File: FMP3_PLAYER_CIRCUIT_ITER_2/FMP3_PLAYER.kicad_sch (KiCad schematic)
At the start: 47 parts, among them J1 USB_C_Receptacle_PowerOnly_6P, J2 AudioJack3, J3 ISP, Q1 PMOS, Q2 PMOS, SW1 SW_L, SW2 SW_D, SW3 SW_R, SW4 SW_U, SW5 SW_SPDT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

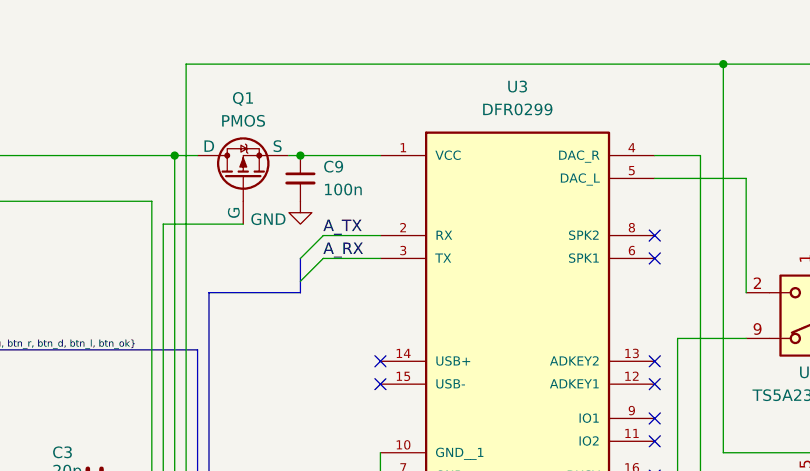
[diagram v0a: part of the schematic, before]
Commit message: The DFPlayer NEEDS a fat decoupling cap...
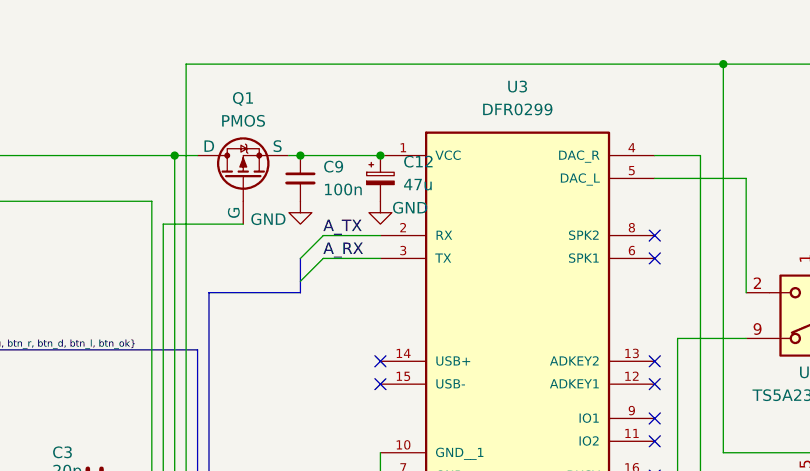
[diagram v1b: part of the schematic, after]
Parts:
- added C12: 47u, Capacitor_THT:CP_Radial_D5.0mm_P2.50mm, symbol Device:C_Polarized_Small
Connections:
- net GND: now also C12.2
- net at C9.1, Q1.3 (S), U3.1 (VCC): now also C12.1
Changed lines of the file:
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@@
 	)
 	(junction
+		(at 208.28 27.94)
+		(diameter 0)
+		(color 0 0 0 0)
+	)
+	(junction
 		(at 185.42 109.22)
 		(diameter 0)
@@
 	)
 	(symbol
+		(lib_id "power:GND")
+		(at 208.28 33.02 0)
+		(unit 1)
+		(exclude_from_sim no)
+		(in_bom yes)
+		(on_board yes)
+		(dnp no)
+		(property "Reference" "#PWR033"
+			(at 208.28 39.37 0)
+			(effects
+				(font
+					(size 1.27 1.27)
+				)
+				(hide yes)
+			)
+		)
+		(property "Value" "GND"
+			(at 211.582 33.782 0)
+			(effects
+				(font
+					(size 1.27 1.27)
+				)
+			)
+		)
+		(property "Footprint" ""
+			(at 208.28 33.02 0)
+			(effects
+				(font
+					(size 1.27 1.27)
+				)
+				(hide yes)
+			)
+		)
+		(property "Datasheet" ""
+			(at 208.28 33.02 0)
+			(effects
+				(font
+					(size 1.27 1.27)
+				)
+				(hide yes)
+			)
+		)
+		(property "Description" "Power symbol creates a global label with name \"GND\" , ground"
+			(at 208.28 33.02 0)
+			(effects
+				(font
+					(size 1.27 1.27)
+				)
+				(hide yes)
+			)
+		)
+		(pin "1"
+		)
+		(instances
+			(project "FMP3_PLAYER"
+				(path "/a3d3848e-8dd1-4cdc-911f-454b6af41ad0"
+					(reference "#PWR033")
+					(unit 1)
+				)
+			)
+		)
+	)
+	(symbol
 		(lib_id "Device:R")
 		(at 189.23 111.76 90)
@@
 					(unit 1)
 				)
+			)
+		)
+	)
+	(symbol
+		(lib_id "Device:C_Polarized_Small")
+		(at 208.28 30.48 0)
+		(unit 1)
+		(exclude_from_sim no)
+		(in_bom yes)
+		(on_board yes)
+		(dnp no)
+		(fields_autoplaced yes)
+		(property "Reference" "C12"
+			(at 210.82 28.6638 0)
+			(effects
+				(font
+					(size 1.27 1.27)
+				)
+				(justify left)
+			)
+		)
+		(property "Value" "47u"
+			(at 210.82 31.2038 0)
+			(effects
+				(font
+					(size 1.27 1.27)
+				)
+				(justify left)
+			)
+		)
+		(property "Footprint" "Capacitor_THT:CP_Radial_D5.0mm_P2.50mm"
+			(at 208.28 30.48 0)
+			(effects
+				(font
+					(size 1.27 1.27)
+				)
+				(hide yes)
+			)
+		)
+		(property "Datasheet" "~"
+			(at 208.28 30.48 0)
+			(effects
+				(font
+					(size 1.27 1.27)
+				)
+				(hide yes)
+			)
+		)
+		(property "Description" "Polarized capacitor, small symbol"
+			(at 208.28 30.48 0)
+			(effects
+				(font
+					(size 1.27 1.27)
+				)
+				(hide yes)
+			)
+		)
+		(pin "2"
+		)
+		(pin "1"
+		)
+		(instances
+			(project ""
+				(path "/a3d3848e-8dd1-4cdc-911f-454b6af41ad0"
+					(reference "C12")
+					(unit 1)
+				)

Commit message: I swear to git this is the final pcb...
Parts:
- added C13, C14: 100n, Capacitor_SMD:C_0805_2012Metric_Pad1.18x1.45mm_HandSolder, symbol Device:C_Small
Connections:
- net at J2.R: now also C14.1; no longer U4.6
- net at J2.T: now also C13.1; no longer U4.10
- new net: C14.2, U4.6
- new net: C13.2, U4.10
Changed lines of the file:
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@@
 	(wire
 		(pts
+			(xy 264.16 27.94) (xy 264.16 40.64)
+		)
+		(stroke
+			(width 0)
+			(type default)
+		)
+	)
+	(wire
+		(pts
 			(xy 233.68 82.55) (xy 241.3 82.55)
 		)
@@
 	(wire
 		(pts
-			(xy 266.7 68.58) (xy 266.7 30.48)
-		)
-		(stroke
-			(width 0)
-			(type default)
-		)
-	)
-	(wire
-		(pts
 			(xy 50.8 36.83) (xy 48.26 36.83)
 		)
@@
 	(wire
 		(pts
-			(xy 264.16 45.72) (xy 264.16 27.94)
-		)
-		(stroke
-			(width 0)
-			(type default)
-		)
-	)
-	(wire
-		(pts
 			(xy 212.09 144.78) (xy 212.09 154.94)
 		)
@@
 	(wire
 		(pts
+			(xy 266.7 30.48) (xy 266.7 63.5)
+		)
+		(stroke
+			(width 0)
+			(type default)
+		)
+	)
+	(wire
+		(pts
 			(xy 149.86 27.94) (xy 185.42 27.94)
 		)
@@
 	(symbol
 		(lib_id "Device:C_Small")
+		(at 266.7 66.04 0)
+		(unit 1)
+		(exclude_from_sim no)
+		(in_bom yes)
+		(on_board yes)
+		(dnp no)
+		(property "Reference" "C14"
+			(at 269.24 64.7762 0)
+			(effects
+				(font
+					(size 1.27 1.27)
+				)
+				(justify left)
+			)
+		)
+		(property "Value" "100n"
+			(at 269.24 67.3162 0)
+			(effects
+				(font
+					(size 1.27 1.27)
+				)
+				(justify left)
+			)
+		)
+		(property "Footprint" "Capacitor_SMD:C_0805_2012Metric_Pad1.18x1.45mm_HandSolder"
+			(at 266.7 66.04 0)
+			(effects
+				(font
+					(size 1.27 1.27)
+				)
+				(hide yes)
+			)
+		)
+		(property "Datasheet" "~"
+			(at 266.7 66.04 0)
+			(effects
+				(font
+					(size 1.27 1.27)
+				)
+				(hide yes)
+			)
+		)
+		(property "Description" "Unpolarized capacitor, small symbol"
+			(at 266.7 66.04 0)
+			(effects
+				(font
+					(size 1.27 1.27)
+				)
+				(hide yes)
+			)
+		)
+		(pin "2"
+		)
+		(pin "1"
+		)
+		(instances
+			(project "FMP3_PLAYER"
+				(path "/a3d3848e-8dd1-4cdc-911f-454b6af41ad0"
+					(reference "C14")
+					(unit 1)
+				)
+			)
+		)
+	)
+	(symbol
+		(lib_id "Device:C_Small")
 		(at 140.97 31.75 90)
 		(unit 1)
@@
 					(unit 1)
 				)
+			)
+		)
+	)
+	(symbol
+		(lib_id "Device:C_Small")
+		(at 264.16 43.18 0)
+		(unit 1)
+		(exclude_from_sim no)
+		(in_bom yes)
+		(on_board yes)
+		(dnp no)
+		(property "Reference" "C13"
+			(at 258.826 37.592 0)
+			(effects
+				(font
+					(size 1.27 1.27)
+				)
+				(justify left)
+			)
+		)
+		(property "Value" "100n"
+			(at 258.826 40.132 0)
+			(effects
+				(font
+					(size 1.27 1.27)
+				)
+				(justify left)
+			)
+		)
+		(property "Footprint" "Capacitor_SMD:C_0805_2012Metric_Pad1.18x1.45mm_HandSolder"
+			(at 264.16 43.18 0)
+			(effects
+				(font
+					(size 1.27 1.27)
+				)
+				(hide yes)
+			)
+		)
+		(property "Datasheet" "~"
+			(at 264.16 43.18 0)
+			(effects
+				(font
+					(size 1.27 1.27)
+				)
+				(hide yes)
+			)
+		)
+		(property "Description" "Unpolarized capacitor, small symbol"
+			(at 264.16 43.18 0)
+			(effects
+				(font
+					(size 1.27 1.27)
+				)
+				(hide yes)
+			)
+		)
+		(pin "2"
+		)
+		(pin "1"
+		)
+		(instances
+			(project "FMP3_PLAYER"
+				(path "/a3d3848e-8dd1-4cdc-911f-454b6af41ad0"
+					(reference "C13")
+					(unit 1)
+				)

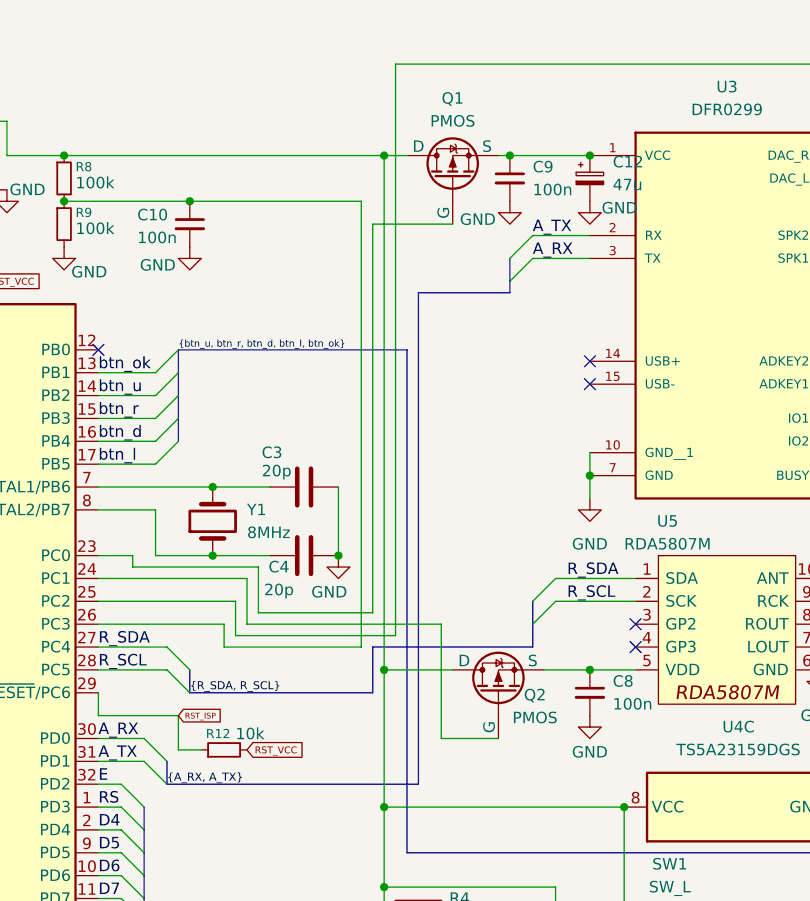
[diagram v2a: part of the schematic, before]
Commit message: I realized after some prototyping my PMOS was bad, fixed now, i swear this better be the final...
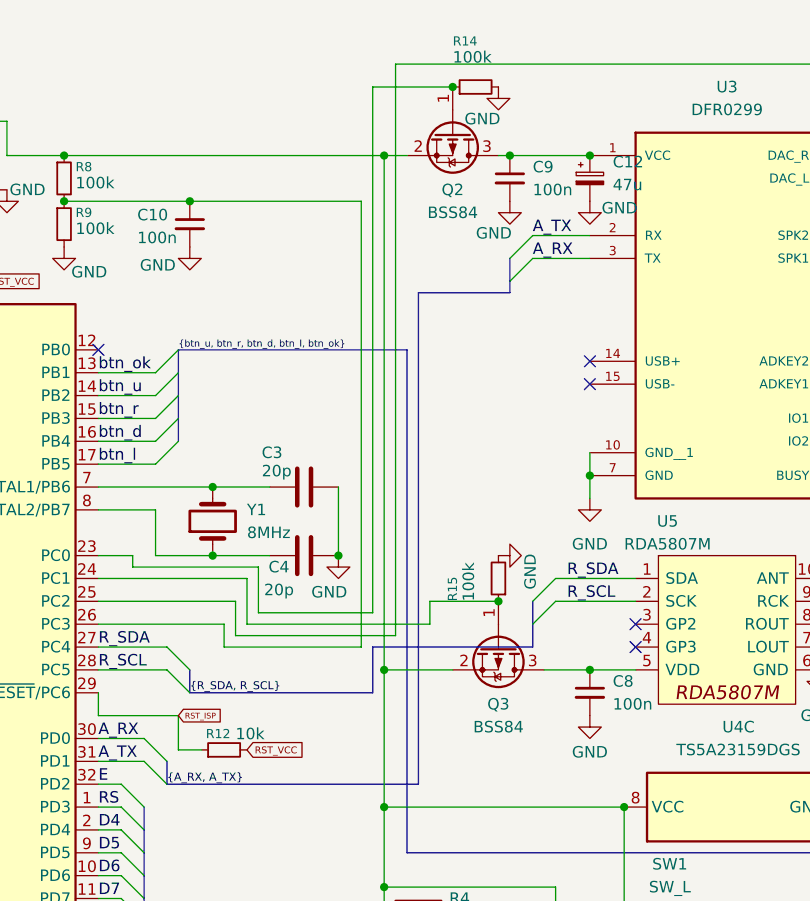
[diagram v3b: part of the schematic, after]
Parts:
- removed Q1, Q2: PMOS, Package_TO_SOT_SMD:SOT-23_Handsoldering, symbol Simulation_SPICE:PMOS
- added Q2, Q3: BSS84, Package_TO_SOT_SMD:SOT-23_Handsoldering, symbol Transistor_FET:BSS84
- added R14, R15: 100k, Resistor_SMD:R_0805_2012Metric_Pad1.20x1.40mm_HandSolder, symbol Device:R_Small
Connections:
- net GND: now also R14.2, R15.2
- net at C8.1, U5.5 (VDD): now also Q3.3 (D)
- net at C5.1, DS1.2 (VDD), R4.1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: now also Q2.2 (S), Q3.2 (S)
- net at U1.23 (PC0): now also Q2.1 (G), R14.1
- net at U1.24 (PC1): now also Q3.1 (G), R15.1
- net at C12.1, C9.1, U3.1 (VCC): now also Q2.3 (D)

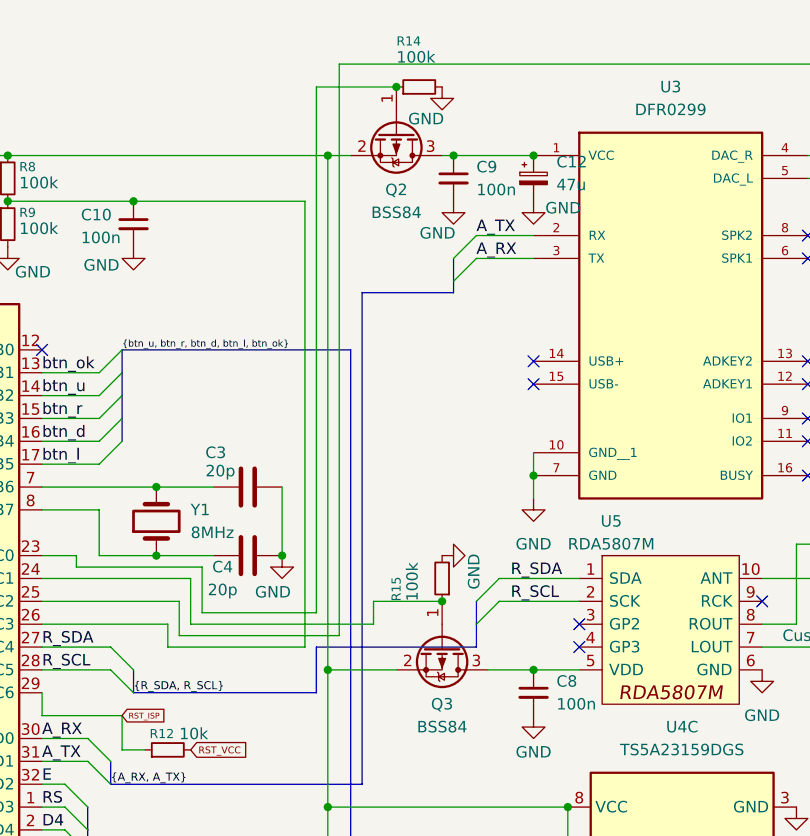
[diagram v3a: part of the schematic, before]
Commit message: minor fix, used pulldowns instead of pullups by accident
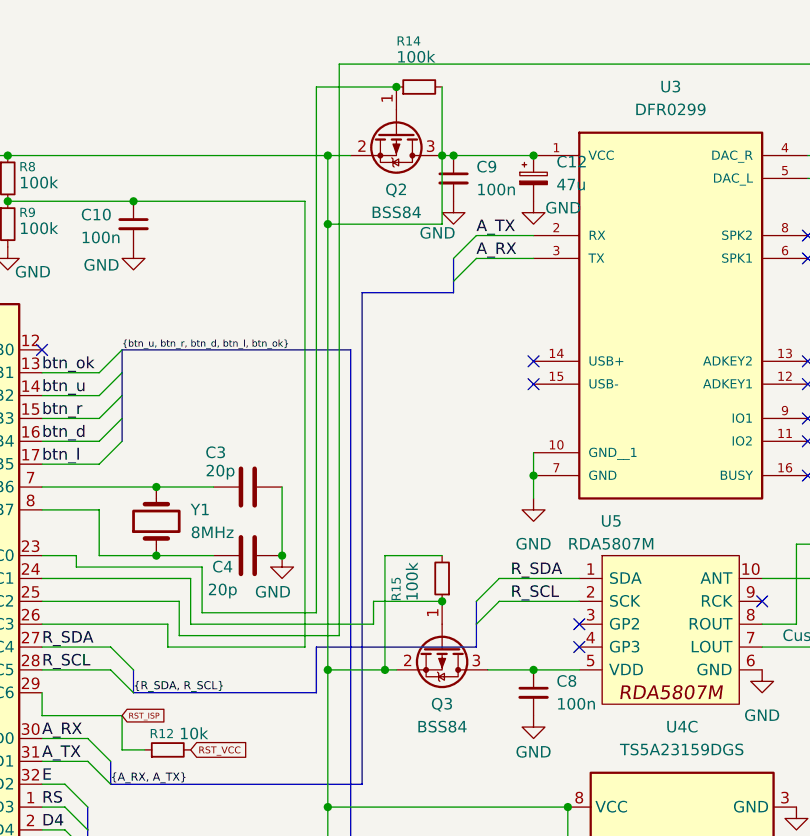
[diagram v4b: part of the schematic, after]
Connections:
- net GND: no longer R14.2, R15.2
- net at C5.1, DS1.2 (VDD), Q2.2 (S)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: now also C12.1, C9.1, Q2.3 (D), R14.2, R15.2, U3.1 (VCC)
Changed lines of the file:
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@@
 	)
 	(junction
+		(at 198.12 27.94)
+		(diameter 0)
+		(color 0 0 0 0)
+	)
+	(junction
 		(at 226.06 134.62)
 		(diameter 0)
@@
 	)
 	(junction
+		(at 191.77 85.09)
+		(diameter 0)
+		(color 0 0 0 0)
+	)
+	(junction
 		(at 208.28 63.5)
 		(diameter 0)
@@
 	)
 	(junction
+		(at 185.42 35.56)
+		(diameter 0)
+		(color 0 0 0 0)
+	)
+	(junction
 		(at 166.37 72.39)
 		(diameter 0)
@@
 	(wire
 		(pts
+			(xy 198.12 27.94) (xy 198.12 35.56)
+		)
+		(stroke
+			(width 0)
+			(type default)
+		)
+	)
+	(wire
+		(pts
 			(xy 168.91 77.47) (xy 168.91 81.28)
 		)
@@
 	(wire
 		(pts
+			(xy 185.42 35.56) (xy 185.42 85.09)
+		)
+		(stroke
+			(width 0)
+			(type default)
+		)
+	)
+	(wire
+		(pts
 			(xy 173.99 119.38) (xy 173.99 123.19)
 		)
@@
 	(wire
 		(pts
+			(xy 191.77 85.09) (xy 193.04 85.09)
+		)
+		(stroke
+			(width 0)
+			(type default)
+		)
+	)
+	(wire
+		(pts
 			(xy 198.12 111.76) (xy 198.12 124.46)
 		)
@@
 	(wire
 		(pts
-			(xy 185.42 85.09) (xy 193.04 85.09)
+			(xy 185.42 85.09) (xy 191.77 85.09)
 		)
 		(stroke
@@
 	(wire
 		(pts
-			(xy 185.42 27.94) (xy 185.42 85.09)
+			(xy 185.42 27.94) (xy 185.42 35.56)
 		)
 		(stroke
@@
 	(wire
 		(pts
+			(xy 191.77 72.39) (xy 191.77 85.09)
+		)
+		(stroke
+			(width 0)
+			(type default)
+		)
+	)
+	(wire
+		(pts
 			(xy 248.92 30.48) (xy 248.92 43.18)
 		)
@@
 	(wire
 		(pts
+			(xy 198.12 72.39) (xy 191.77 72.39)
+		)
+		(stroke
+			(width 0)
+			(type default)
+		)
+	)
+	(wire
+		(pts
 			(xy 233.68 133.35) (xy 233.68 144.78)
 		)
@@
 	(wire
 		(pts
+			(xy 198.12 20.32) (xy 198.12 27.94)
+		)
+		(stroke
+			(width 0)
+			(type default)
+		)
+	)
+	(wire
+		(pts
 			(xy 153.67 62.23) (xy 160.02 62.23)
 		)
@@
 	(wire
 		(pts
+			(xy 198.12 35.56) (xy 185.42 35.56)
+		)
+		(stroke
+			(width 0)
+			(type default)
+		)
+	)
+	(wire
+		(pts
 			(xy 149.86 27.94) (xy 185.42 27.94)
 		)
@@
 	(symbol
 		(lib_id "power:GND")
-		(at 198.12 20.32 0)
-		(unit 1)
-		(exclude_from_sim no)
-		(in_bom yes)
-		(on_board yes)
-		(dnp no)
-		(property "Reference" "#PWR034"
-			(at 198.12 26.67 0)
-			(effects
-				(font
-					(size 1.27 1.27)
-				)
-				(hide yes)
-			)
-		)
-		(property "Value" "GND"
-			(at 196.342 23.876 0)
-			(effects
-				(font
-					(size 1.27 1.27)
-				)
-			)
-		)
-		(property "Footprint" ""
-			(at 198.12 20.32 0)
-			(effects
-				(font
-					(size 1.27 1.27)
-				)
-				(hide yes)
-			)
-		)
-		(property "Datasheet" ""
-			(at 198.12 20.32 0)
-			(effects
-				(font
-					(size 1.27 1.27)
-				)
-				(hide yes)
-			)
-		)
-		(property "Description" "Power symbol creates a global label with name \"GND\" , ground"
-			(at 198.12 20.32 0)
-			(effects
-				(font
-					(size 1.27 1.27)
-				)
-				(hide yes)
-			)
-		)
-		(pin "1"
-		)
-		(instances
-			(project "FMP3_PLAYER"
-				(path "/a3d3848e-8dd1-4cdc-911f-454b6af41ad0"
-					(reference "#PWR034")
-					(unit 1)
-				)
-			)
-		)
-	)
-	(symbol
-		(lib_id "power:GND")
 		(at 208.28 33.02 0)
 		(unit 1)
@@
 					(unit 1)
 				)
-			)
-		)
-	)
-	(symbol
-		(lib_id "power:GND")
-		(at 198.12 72.39 90)
-		(unit 1)
-		(exclude_from_sim no)
-		(in_bom yes)
-		(on_board yes)
-		(dnp no)
-		(property "Reference" "#PWR035"
-			(at 204.47 72.39 0)
-			(effects
-				(font
-					(size 1.27 1.27)
-				)
-				(hide yes)
-			)
-		)
-		(property "Value" "GND"
-			(at 201.676 74.168 0)
-			(effects
-				(font
-					(size 1.27 1.27)
-				)
-			)
-		)
-		(property "Footprint" ""
-			(at 198.12 72.39 0)
-			(effects
-				(font
-					(size 1.27 1.27)
-				)
-				(hide yes)
-			)
-		)
-		(property "Datasheet" ""
-			(at 198.12 72.39 0)
-			(effects
-				(font
-					(size 1.27 1.27)
-				)
-				(hide yes)
-			)
-		)
-		(property "Description" "Power symbol creates a global label with name \"GND\" , ground"
-			(at 198.12 72.39 0)
-			(effects
-				(font
-					(size 1.27 1.27)
-				)
-				(hide yes)
-			)
-		)
-		(pin "1"
-		)
-		(instances
-			(project "FMP3_PLAYER"
-				(path "/a3d3848e-8dd1-4cdc-911f-454b6af41ad0"
-					(reference "#PWR035")
-					(unit 1)
-				)

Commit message: another minor fix, i should really go sleep...
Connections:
- net at C5.1, DS1.2 (VDD), Q2.2 (S)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: no longer C12.1, C9.1, Q2.3 (D), U3.1 (VCC)
- new net: C12.1, C9.1, Q2.3 (D), U3.1 (VCC)
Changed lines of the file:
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@@
-	)
-	(junction
-		(at 198.12 27.94)
-		(diameter 0)
-		(color 0 0 0 0)
 	)
 	(junction
@@
 	(wire
 		(pts
-			(xy 198.12 27.94) (xy 198.12 35.56)
+			(xy 201.93 20.32) (xy 201.93 35.56)
 		)
 		(stroke
@@
 	(wire
 		(pts
-			(xy 198.12 20.32) (xy 198.12 27.94)
-		)
-		(stroke
-			(width 0)
-			(type default)
-		)
-	)
-	(wire
-		(pts
 			(xy 153.67 62.23) (xy 160.02 62.23)
 		)
@@
 	(wire
 		(pts
-			(xy 198.12 35.56) (xy 185.42 35.56)
+			(xy 201.93 35.56) (xy 185.42 35.56)
 		)
 		(stroke
@@
 		)
 		(stroke
+			(width 0)
+			(type default)
+		)
+	)
+	(wire
+		(pts
+			(xy 201.93 20.32) (xy 198.12 20.32)
+		)
+		(stroke
